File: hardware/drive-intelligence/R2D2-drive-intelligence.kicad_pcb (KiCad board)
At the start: 2 copper layers, 25.5 x 28 mm, 36 parts, among them J1 Conn_01x05_Pin, J2 1751248, J3 1751248, J4 1751248, J5 1725669, SW1 PTS636 SM50J SMTR LFS, U1 STM32F042F6Px, U2 SN65HVD230, U3 LM1117MP-3.3, U4 LMV321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

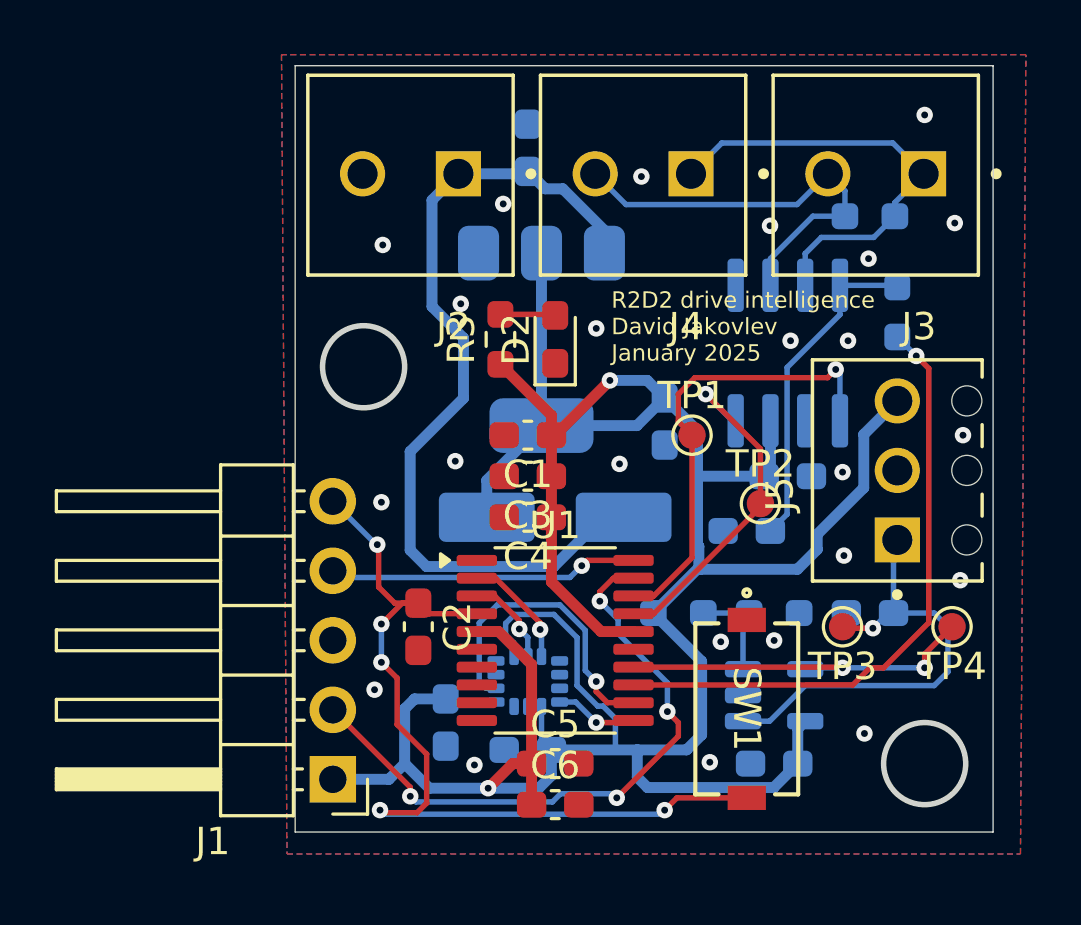
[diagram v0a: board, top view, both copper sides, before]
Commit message: hw: drive-intelligence: added solder jumper for left or right motor setting
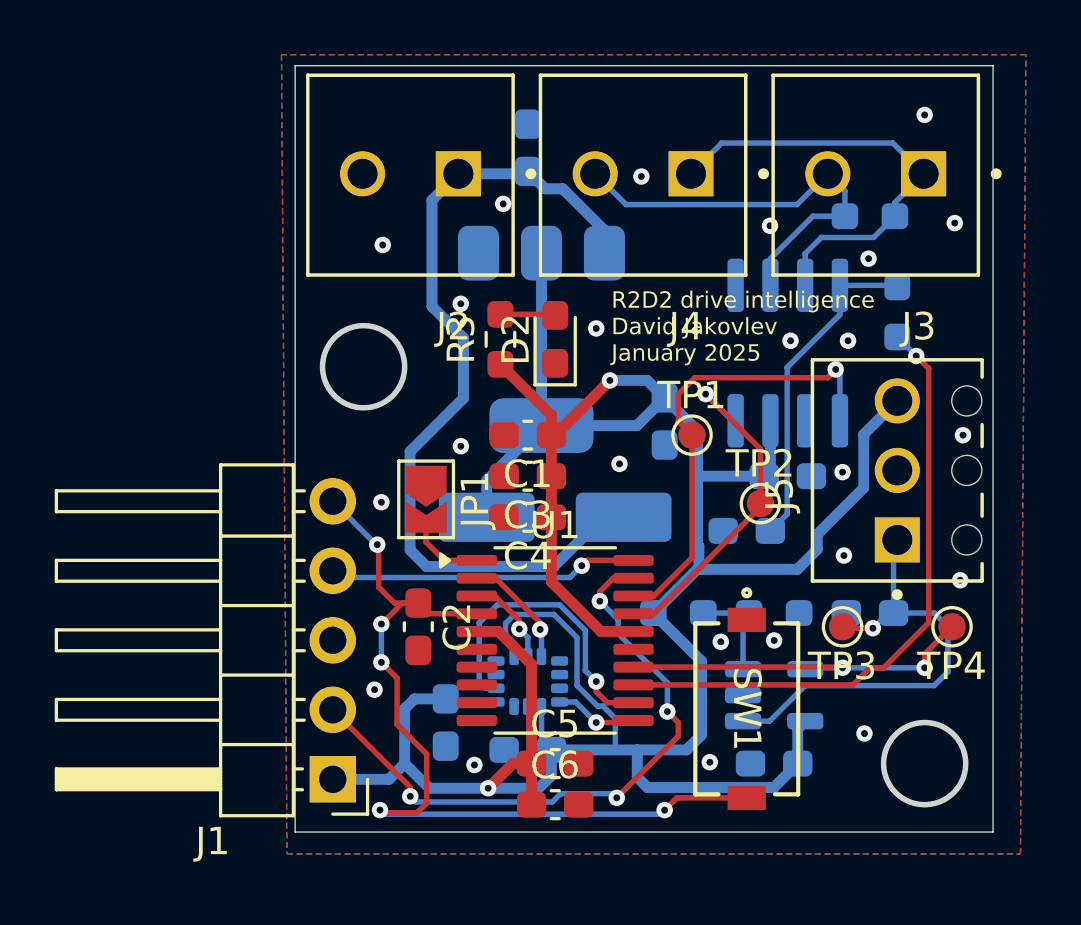
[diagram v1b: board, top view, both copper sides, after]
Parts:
- added JP1: CAN address, Jumper:SolderJumper-2_P1.3mm_Open_TrianglePad1.0x1.5mm, F.Cu at (113.3, 71.8)
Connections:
- U1 pad 1: unconnected-(U1-PB8-Pad1) -> Net-(JP1-B)
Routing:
- net Net-(JP1-B): track 0.00 -> 2.97 mm
